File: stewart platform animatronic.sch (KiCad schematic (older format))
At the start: 23 parts, among them P1 CONN_01X03, P10 CONN_01X03, P11 CONN_01X03, P12 CONN_01X03, P13 CONN_01X02, P14 CONN_01X03, P15 CONN_01X03, P16 CONN_01X03, P17 CONN_01X03, P18 CONN_01X03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

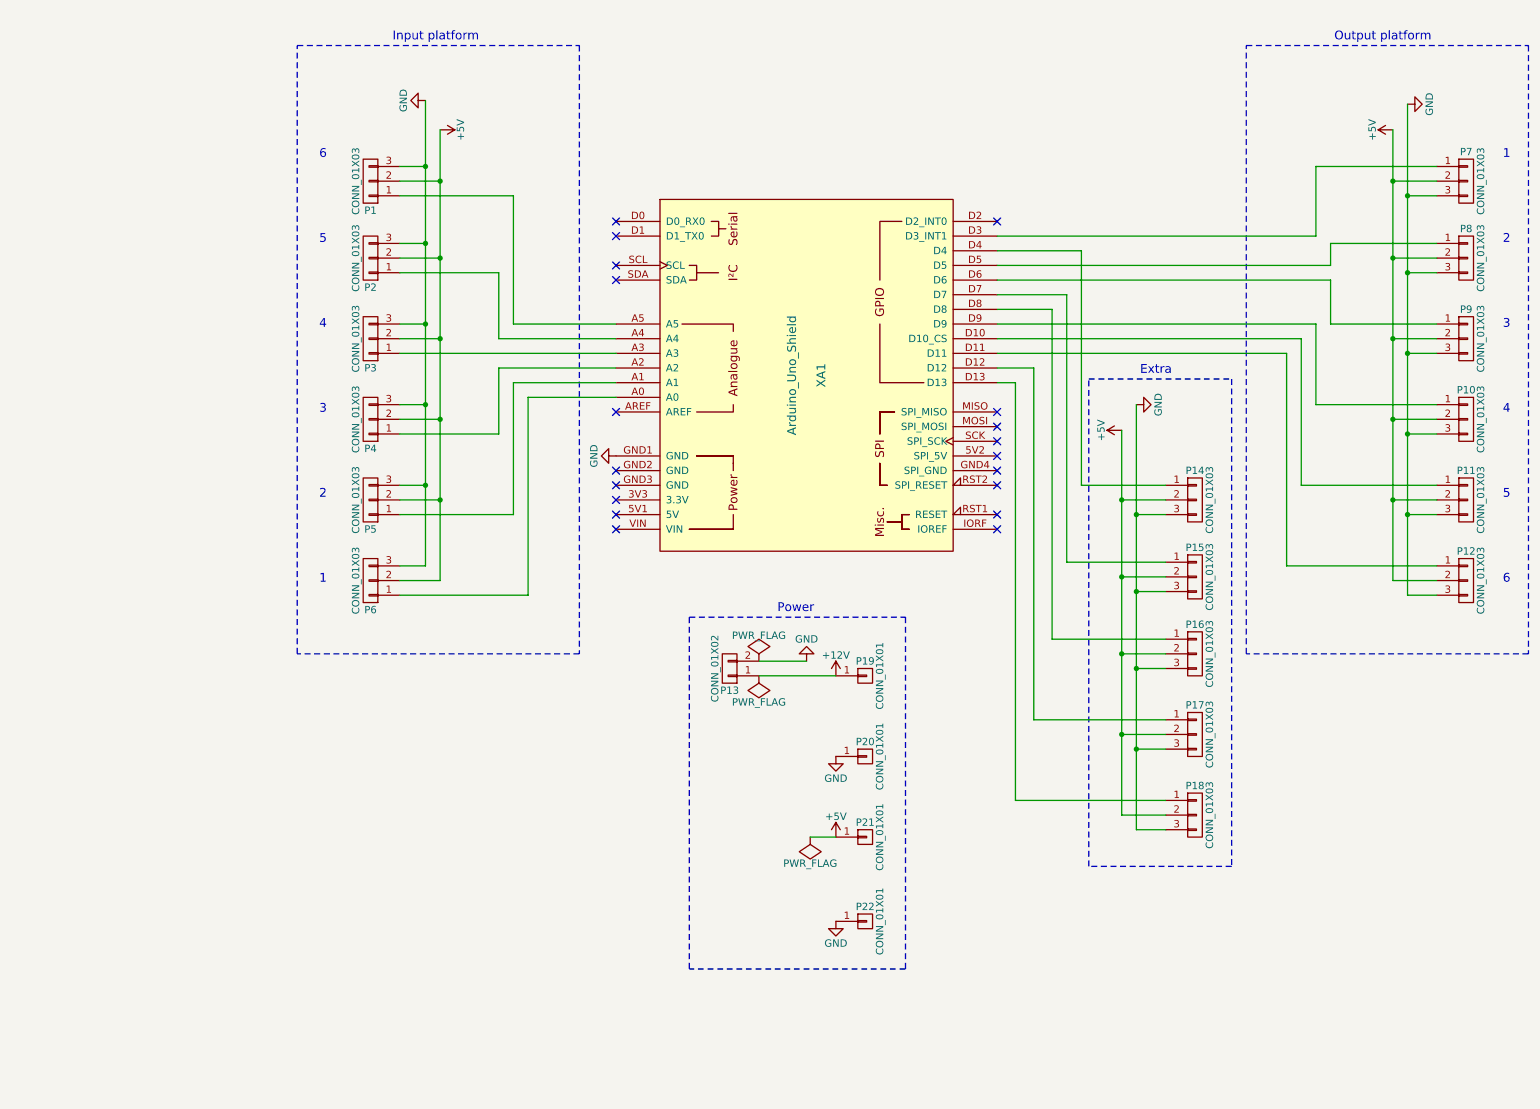
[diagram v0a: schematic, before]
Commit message: updated PCB for MEGA
for MEGA design
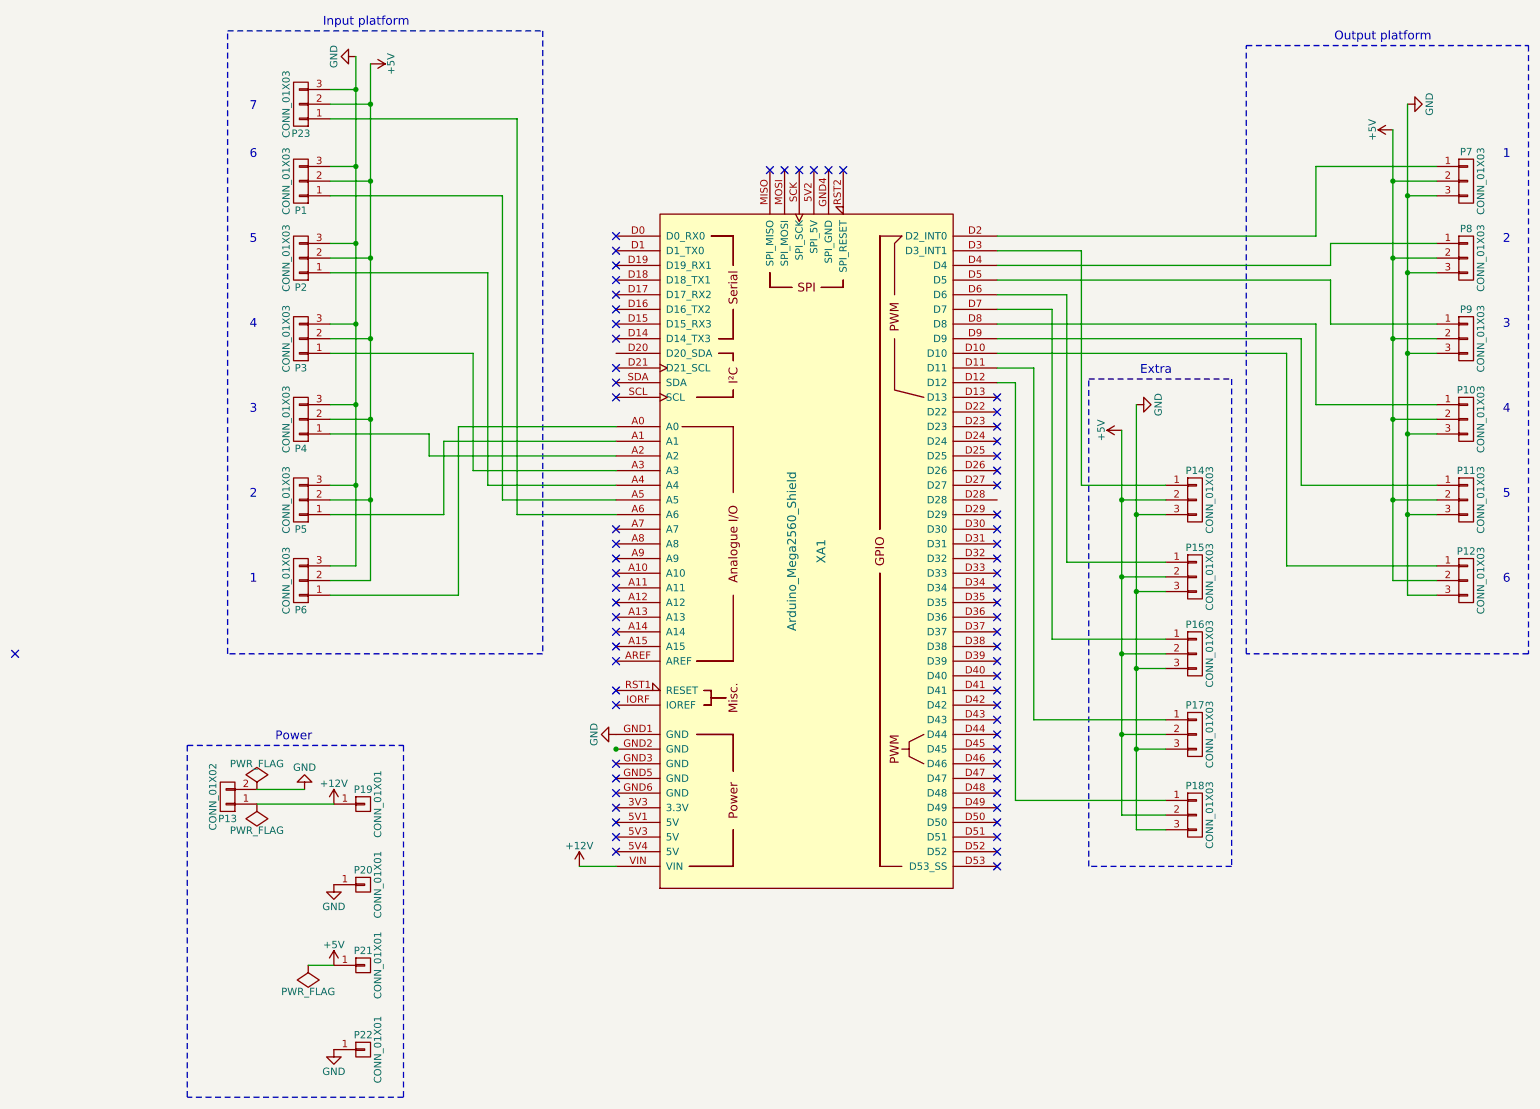
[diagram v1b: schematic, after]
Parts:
- removed XA1: Arduino_Uno_Shield, Arduino:Arduino_Uno_Shield, symbol Arduino_Uno_Shield
- added P23: CONN_01X03, Socket_Strips:Socket_Strip_Straight_1x03_Pitch2.54mm, symbol CONN_01X03
- added XA1: Arduino_Mega2560_Shield, Arduino:Arduino_Mega2560_Shield, symbol Arduino_Mega2560_Shield
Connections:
- net +12V: now also XA1.VIN
- net +5V: now also P23.2 (P2)
- net GND: now also P23.3 (P3), XA1.GND1 (GND)
- net at P7.1 (P1): now also XA1.D2 (D2_INT0)
- net at P8.1 (P1): now also XA1.D4
- net at P9.1 (P1): now also XA1.D5
- net at P10.1 (P1): now also XA1.D8
- net at P11.1 (P1): now also XA1.D9
- net at P12.1 (P1): now also XA1.D10
- net at P1.1 (P1): now also XA1.A5
- net at P2.1 (P1): now also XA1.A4
- net at P3.1 (P1): now also XA1.A3
- net at P4.1 (P1): now also XA1.A2
- net at P5.1 (P1): now also XA1.A1
- net at P6.1 (P1): now also XA1.A0
- net at P17.1 (P1): now also XA1.D11
- net at P18.1 (P1): now also XA1.D12
- net at P14.1 (P1): now also XA1.D3 (D3_INT1)
- net at P15.1 (P1): now also XA1.D6
- net at P16.1 (P1): now also XA1.D7
- new net: P23.1 (P1), XA1.A6
- no-connect marks 19 -> 69
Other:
- note added: "7"
- moved on the sheet: P1, P13, P19, P2, P20, P21, P22, P3, P4, P5, P6
